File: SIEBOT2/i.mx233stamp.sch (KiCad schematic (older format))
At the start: 0 parts

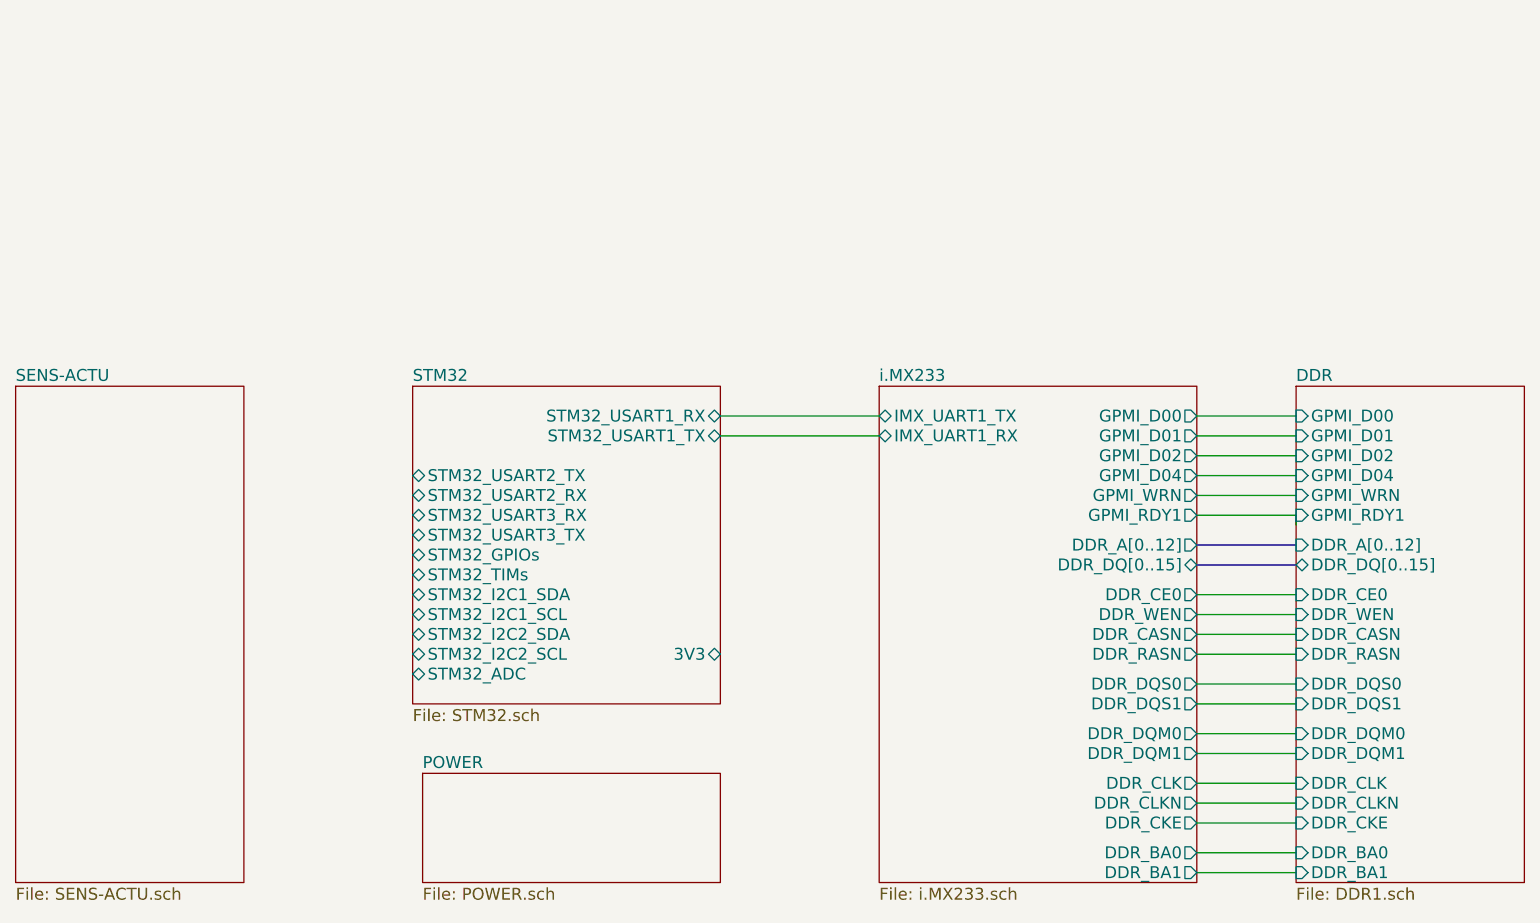
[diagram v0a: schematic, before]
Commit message: Added some fixes from AndroidStamp
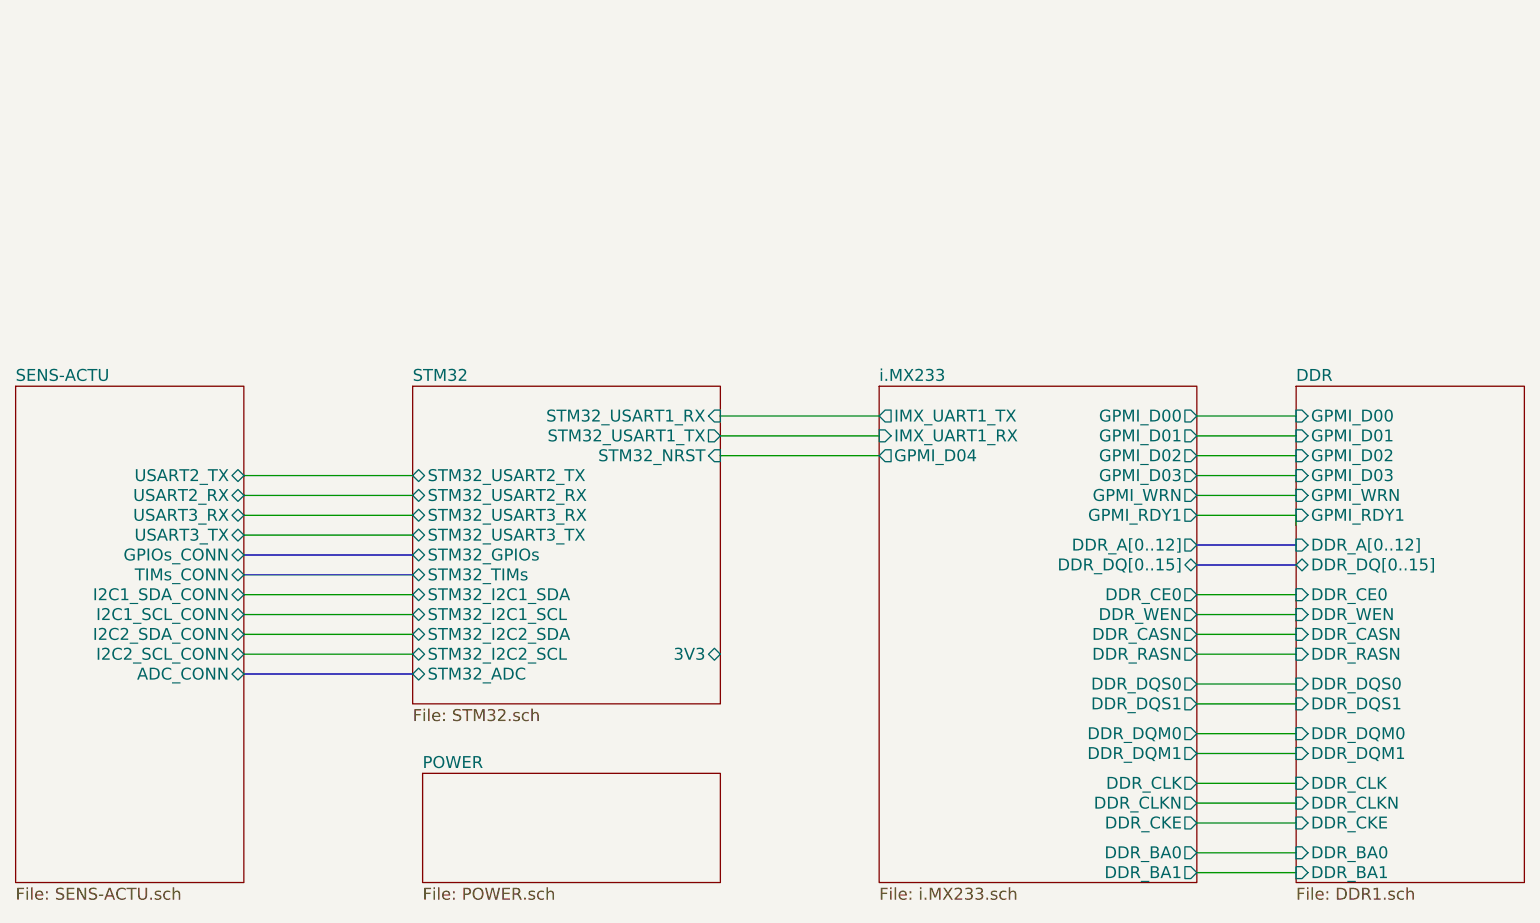
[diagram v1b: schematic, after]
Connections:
- wire segments 22 -> 31
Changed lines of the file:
@@
-EESchema Schematic File Version 2  date sáb 05 mar 2011 23:35:11 COT
+EESchema Schematic File Version 2  date jue 07 abr 2011 23:57:53 COT
 LIBS:stm32f100vxx
 LIBS:transistor-npn
@@
 LIBS:PROpendous-cache
 LIBS:w_analog
+LIBS:adm3101e
 LIBS:i.mx233stamp-cache
 EELAYER 25  0
@@
 Sheet 1 6
 Title ""
-Date "6 mar 2011"
+Date "8 apr 2011"
 Rev ""
 Comp ""
@@
 $EndDescr
 Wire Wire Line
+	6450 3250 5650 3250
+Wire Wire Line
+	3250 4250 4100 4250
+Wire Wire Line
+	4100 4050 3250 4050
+Wire Bus Line
+	4100 3750 3250 3750
+Wire Wire Line
+	4100 3650 3250 3650
+Wire Wire Line
+	4100 3450 3250 3450
+Wire Wire Line
 	5650 3150 6450 3150
 Wire Wire Line
@@
 Wire Wire Line
 	5650 3050 6450 3050
+Wire Wire Line
+	3250 3350 4100 3350
+Wire Wire Line
+	3250 3550 4100 3550
+Wire Bus Line
+	3250 3850 4100 3850
+Wire Wire Line
+	4100 3950 3250 3950
+Wire Wire Line
+	3250 4150 4100 4150
+Wire Bus Line
+	4100 4350 3250 4350
 $Sheet
 S 4100 2900 1550 1600
@@
 F0 "STM32" 60
 F1 "STM32.sch" 60
-F2 "STM32_USART1_RX" B R 5650 3050 60
+F2 "STM32_USART1_RX" I R 5650 3050 60
 F3 "STM32_ADC" B L 4100 4350 60
 F4 "3V3" B R 5650 4250 60
-F5 "STM32_USART1_TX" B R 5650 3150 60
+F5 "STM32_USART1_TX" O R 5650 3150 60
 F6 "STM32_I2C2_SCL" B L 4100 4250 60
 F7 "STM32_I2C2_SDA" B L 4100 4150 60
@@
 F14 "STM32_USART2_RX" B L 4100 3450 60
 F15 "STM32_USART2_TX" B L 4100 3350 60
+F16 "STM32_NRST" I R 5650 3250 60
 $EndSheet
 $Sheet
@@
 F0 "SENS-ACTU" 60
 F1 "SENS-ACTU.sch" 60
+F2 "USART3_RX" B R 3250 3550 60
+F3 "USART3_TX" B R 3250 3650 60
+F4 "USART2_TX" B R 3250 3350 60
+F5 "USART2_RX" B R 3250 3450 60
+F6 "GPIOs_CONN" B R 3250 3750 60
+F7 "TIMs_CONN" B R 3250 3850 60
+F8 "I2C2_SDA_CONN" B R 3250 4150 60
+F9 "I2C2_SCL_CONN" B R 3250 4250 60
+F10 "I2C1_SDA_CONN" B R 3250 3950 60
+F11 "I2C1_SCL_CONN" B R 3250 4050 60
+F12 "ADC_CONN" B R 3250 4350 60
 $EndSheet
 $Sheet
@@
 F15 "DDR_RASN" I L 8550 4250 60
 F16 "DDR_WEN" I L 8550 4050 60
-F17 "GPMI_D04" I L 8550 3350 60
+F17 "GPMI_D03" I L 8550 3350 60
 F18 "GPMI_D02" I L 8550 3250 60
 F19 "GPMI_WRN" I L 8550 3450 60
@@
 F15 "DDR_BA1" O R 8050 5350 60
 F16 "DDR_BA0" O R 8050 5250 60
-F17 "GPMI_D04" O R 8050 3350 60
+F17 "GPMI_D03" O R 8050 3350 60
 F18 "GPMI_WRN" O R 8050 3450 60
 F19 "GPMI_RDY1" O R 8050 3550 60
@@
 F21 "GPMI_D01" O R 8050 3150 60
 F22 "GPMI_D02" O R 8050 3250 60
-F23 "IMX_UART1_TX" B L 6450 3050 60
-F24 "IMX_UART1_RX" B L 6450 3150 60
+F23 "IMX_UART1_TX" O L 6450 3050 60
+F24 "IMX_UART1_RX" I L 6450 3150 60
+F25 "GPMI_D04" O L 6450 3250 60
 $EndSheet
 $EndSCHEMATC

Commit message: Added power dc-dc, fixed stm32 control pins
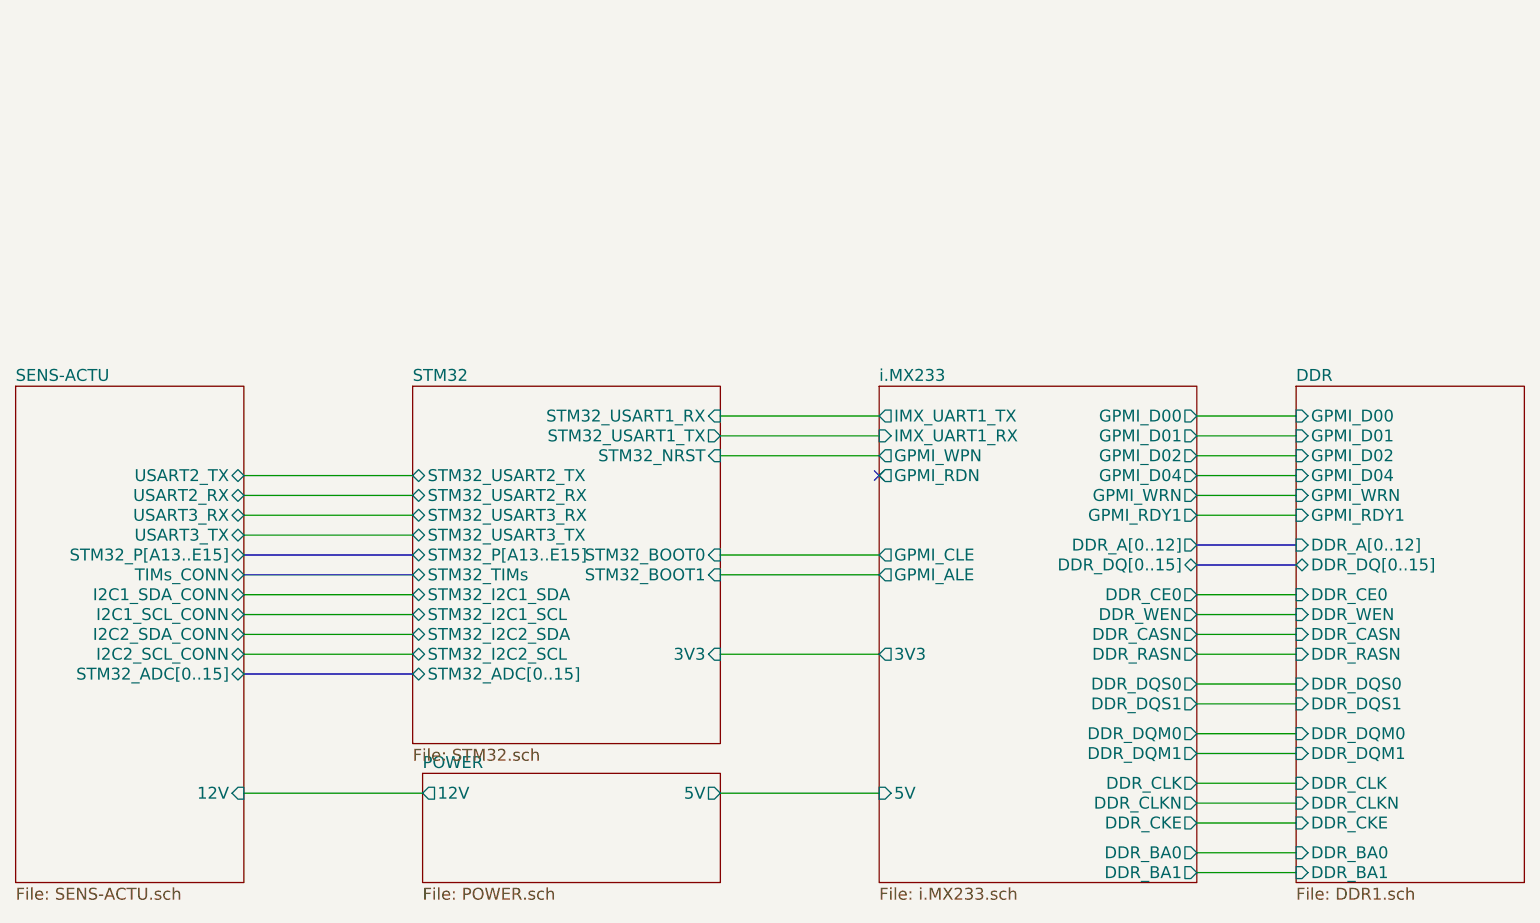
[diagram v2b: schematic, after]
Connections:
- no-connect marks 0 -> 1
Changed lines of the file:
@@
-EESchema Schematic File Version 2  date jue 07 abr 2011 23:57:53 COT
+EESchema Schematic File Version 2  date lun 11 abr 2011 13:13:06 COT
+LIBS:dc-dc
 LIBS:stm32f100vxx
 LIBS:transistor-npn
@@
 Sheet 1 6
 Title ""
-Date "8 apr 2011"
+Date "11 apr 2011"
 Rev ""
 Comp ""
@@
 $EndDescr
 Wire Wire Line
+	6450 4950 5650 4950
+Wire Wire Line
+	6450 4250 5650 4250
+Wire Wire Line
+	5650 3750 6450 3750
+Wire Bus Line
+	4100 4350 3250 4350
+Wire Wire Line
+	3250 4150 4100 4150
+Wire Wire Line
+	4100 3950 3250 3950
+Wire Bus Line
+	3250 3850 4100 3850
+Wire Wire Line
+	3250 3550 4100 3550
+Wire Wire Line
+	3250 3350 4100 3350
+Wire Wire Line
+	5650 3050 6450 3050
+Wire Wire Line
+	8550 3550 8050 3550
+Wire Wire Line
+	8550 3250 8050 3250
+Wire Wire Line
+	8550 3050 8050 3050
+Wire Bus Line
+	8550 3700 8050 3700
+Wire Wire Line
+	8050 4750 8550 4750
+Wire Wire Line
+	8550 4500 8050 4500
+Wire Wire Line
+	8050 4250 8550 4250
+Wire Wire Line
+	8050 5350 8550 5350
+Wire Wire Line
+	8050 5100 8550 5100
+Wire Wire Line
+	8050 4900 8550 4900
+Wire Wire Line
+	8050 4150 8550 4150
+Wire Wire Line
+	8050 4050 8550 4050
+Wire Wire Line
+	8050 3950 8550 3950
+Wire Wire Line
+	8050 5000 8550 5000
+Wire Wire Line
+	8050 5250 8550 5250
+Wire Wire Line
+	8050 4400 8550 4400
+Wire Wire Line
+	8550 4650 8050 4650
+Wire Wire Line
+	8050 3350 8550 3350
+Wire Bus Line
+	8050 3800 8550 3800
+Wire Wire Line
+	8050 3150 8550 3150
+Wire Wire Line
+	8050 3450 8550 3450
+Wire Wire Line
+	5650 3150 6450 3150
+Wire Wire Line
+	4100 3450 3250 3450
+Wire Wire Line
+	4100 3650 3250 3650
+Wire Bus Line
+	4100 3750 3250 3750
+Wire Wire Line
+	4100 4050 3250 4050
+Wire Wire Line
+	3250 4250 4100 4250
+Wire Wire Line
 	6450 3250 5650 3250
 Wire Wire Line
-	3250 4250 4100 4250
-Wire Wire Line
-	4100 4050 3250 4050
-Wire Bus Line
-	4100 3750 3250 3750
-Wire Wire Line
-	4100 3650 3250 3650
-Wire Wire Line
-	4100 3450 3250 3450
-Wire Wire Line
-	5650 3150 6450 3150
-Wire Wire Line
-	8050 3450 8550 3450
-Wire Wire Line
-	8050 3150 8550 3150
-Wire Bus Line
-	8050 3800 8550 3800
-Wire Wire Line
-	8050 3350 8550 3350
-Wire Wire Line
-	8550 4650 8050 4650
-Wire Wire Line
-	8050 4400 8550 4400
-Wire Wire Line
-	8050 5250 8550 5250
-Wire Wire Line
-	8050 5000 8550 5000
-Wire Wire Line
-	8050 3950 8550 3950
-Wire Wire Line
-	8050 4050 8550 4050
-Wire Wire Line
-	8050 4150 8550 4150
-Wire Wire Line
-	8050 4900 8550 4900
-Wire Wire Line
-	8050 5100 8550 5100
-Wire Wire Line
-	8050 5350 8550 5350
-Wire Wire Line
-	8050 4250 8550 4250
-Wire Wire Line
-	8550 4500 8050 4500
-Wire Wire Line
-	8050 4750 8550 4750
-Wire Bus Line
-	8550 3700 8050 3700
-Wire Wire Line
-	8550 3050 8050 3050
-Wire Wire Line
-	8550 3250 8050 3250
-Wire Wire Line
-	8550 3600 8550 3550
-Wire Wire Line
-	8550 3550 8050 3550
-Wire Wire Line
-	5650 3050 6450 3050
-Wire Wire Line
-	3250 3350 4100 3350
-Wire Wire Line
-	3250 3550 4100 3550
-Wire Bus Line
-	3250 3850 4100 3850
-Wire Wire Line
-	4100 3950 3250 3950
-Wire Wire Line
-	3250 4150 4100 4150
-Wire Bus Line
-	4100 4350 3250 4350
-$Sheet
-S 4100 2900 1550 1600
+	6450 3850 5650 3850
+Wire Wire Line
+	4150 4950 3250 4950
+NoConn ~ 6450 3350
+$Sheet
+S 4100 2900 1550 1800
 U 4D6EB053
 F0 "STM32" 60
 F1 "STM32.sch" 60
 F2 "STM32_USART1_RX" I R 5650 3050 60
-F3 "STM32_ADC" B L 4100 4350 60
-F4 "3V3" B R 5650 4250 60
-F5 "STM32_USART1_TX" O R 5650 3150 60
-F6 "STM32_I2C2_SCL" B L 4100 4250 60
-F7 "STM32_I2C2_SDA" B L 4100 4150 60
-F8 "STM32_I2C1_SDA" B L 4100 3950 60
-F9 "STM32_I2C1_SCL" B L 4100 4050 60
-F10 "STM32_TIMs" B L 4100 3850 60
-F11 "STM32_GPIOs" B L 4100 3750 60
-F12 "STM32_USART3_TX" B L 4100 3650 60
-F13 "STM32_USART3_RX" B L 4100 3550 60
-F14 "STM32_USART2_RX" B L 4100 3450 60
-F15 "STM32_USART2_TX" B L 4100 3350 60
-F16 "STM32_NRST" I R 5650 3250 60
+F3 "STM32_ADC[0..15]" B L 4100 4350 60
+F4 "STM32_USART1_TX" O R 5650 3150 60
+F5 "STM32_I2C2_SCL" B L 4100 4250 60
+F6 "STM32_I2C2_SDA" B L 4100 4150 60
+F7 "STM32_I2C1_SDA" B L 4100 3950 60
+F8 "STM32_I2C1_SCL" B L 4100 4050 60
+F9 "STM32_TIMs" B L 4100 3850 60
+F10 "STM32_P[A13..E15]" B L 4100 3750 60
+F11 "STM32_USART3_TX" B L 4100 3650 60
+F12 "STM32_USART3_RX" B L 4100 3550 60
+F13 "STM32_USART2_RX" B L 4100 3450 60
+F14 "STM32_USART2_TX" B L 4100 3350 60
+F15 "STM32_NRST" I R 5650 3250 60
+F16 "STM32_BOOT0" I R 5650 3750 60
+F17 "STM32_BOOT1" I R 5650 3850 60
+F18 "3V3" I R 5650 4250 60
 $EndSheet
 $Sheet
@@
 F4 "USART2_TX" B R 3250 3350 60
 F5 "USART2_RX" B R 3250 3450 60
-F6 "GPIOs_CONN" B R 3250 3750 60
+F6 "STM32_P[A13..E15]" B R 3250 3750 60
 F7 "TIMs_CONN" B R 3250 3850 60
 F8 "I2C2_SDA_CONN" B R 3250 4150 60
@@
 F10 "I2C1_SDA_CONN" B R 3250 3950 60
 F11 "I2C1_SCL_CONN" B R 3250 4050 60
-F12 "ADC_CONN" B R 3250 4350 60
+F12 "STM32_ADC[0..15]" B R 3250 4350 60
+F13 "12V" I R 3250 4950 60
 $EndSheet
 $Sheet
@@
 F0 "POWER" 60
 F1 "POWER.sch" 60
+F2 "12V" O L 4150 4950 60
+F3 "5V" O R 5650 4950 60
 $EndSheet
 $Sheet
@@
 F15 "DDR_RASN" I L 8550 4250 60
 F16 "DDR_WEN" I L 8550 4050 60
-F17 "GPMI_D03" I L 8550 3350 60
-F18 "GPMI_D02" I L 8550 3250 60
-F19 "GPMI_WRN" I L 8550 3450 60
-F20 "GPMI_RDY1" I L 8550 3550 60
-F21 "GPMI_D01" I L 8550 3150 60
-F22 "GPMI_D00" I L 8550 3050 60
+F17 "GPMI_D02" I L 8550 3250 60
+F18 "GPMI_WRN" I L 8550 3450 60
+F19 "GPMI_RDY1" I L 8550 3550 60
+F20 "GPMI_D01" I L 8550 3150 60
+F21 "GPMI_D00" I L 8550 3050 60
+F22 "GPMI_D04" I L 8550 3350 60
 $EndSheet
 $Sheet
@@
 F15 "DDR_BA1" O R 8050 5350 60
 F16 "DDR_BA0" O R 8050 5250 60
-F17 "GPMI_D03" O R 8050 3350 60
-F18 "GPMI_WRN" O R 8050 3450 60
-F19 "GPMI_RDY1" O R 8050 3550 60
-F20 "GPMI_D00" O R 8050 3050 60
-F21 "GPMI_D01" O R 8050 3150 60
-F22 "GPMI_D02" O R 8050 3250 60
-F23 "IMX_UART1_TX" O L 6450 3050 60
-F24 "IMX_UART1_RX" I L 6450 3150 60
-F25 "GPMI_D04" O L 6450 3250 60
+F17 "GPMI_WRN" O R 8050 3450 60
+F18 "GPMI_RDY1" O R 8050 3550 60
+F19 "GPMI_D00" O R 8050 3050 60
+F20 "GPMI_D01" O R 8050 3150 60
+F21 "GPMI_D02" O R 8050 3250 60
+F22 "IMX_UART1_TX" O L 6450 3050 60
+F23 "IMX_UART1_RX" I L 6450 3150 60
+F24 "GPMI_WPN" O L 6450 3250 60
+F25 "GPMI_RDN" O L 6450 3350 60
+F26 "GPMI_CLE" O L 6450 3750 60
+F27 "GPMI_ALE" O L 6450 3850 60
+F28 "GPMI_D04" O R 8050 3350 60
+F29 "3V3" O L 6450 4250 60
+F30 "5V" I L 6450 4950 60
 $EndSheet
 $EndSCHEMATC

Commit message: STM32 connection fixes + various fixes
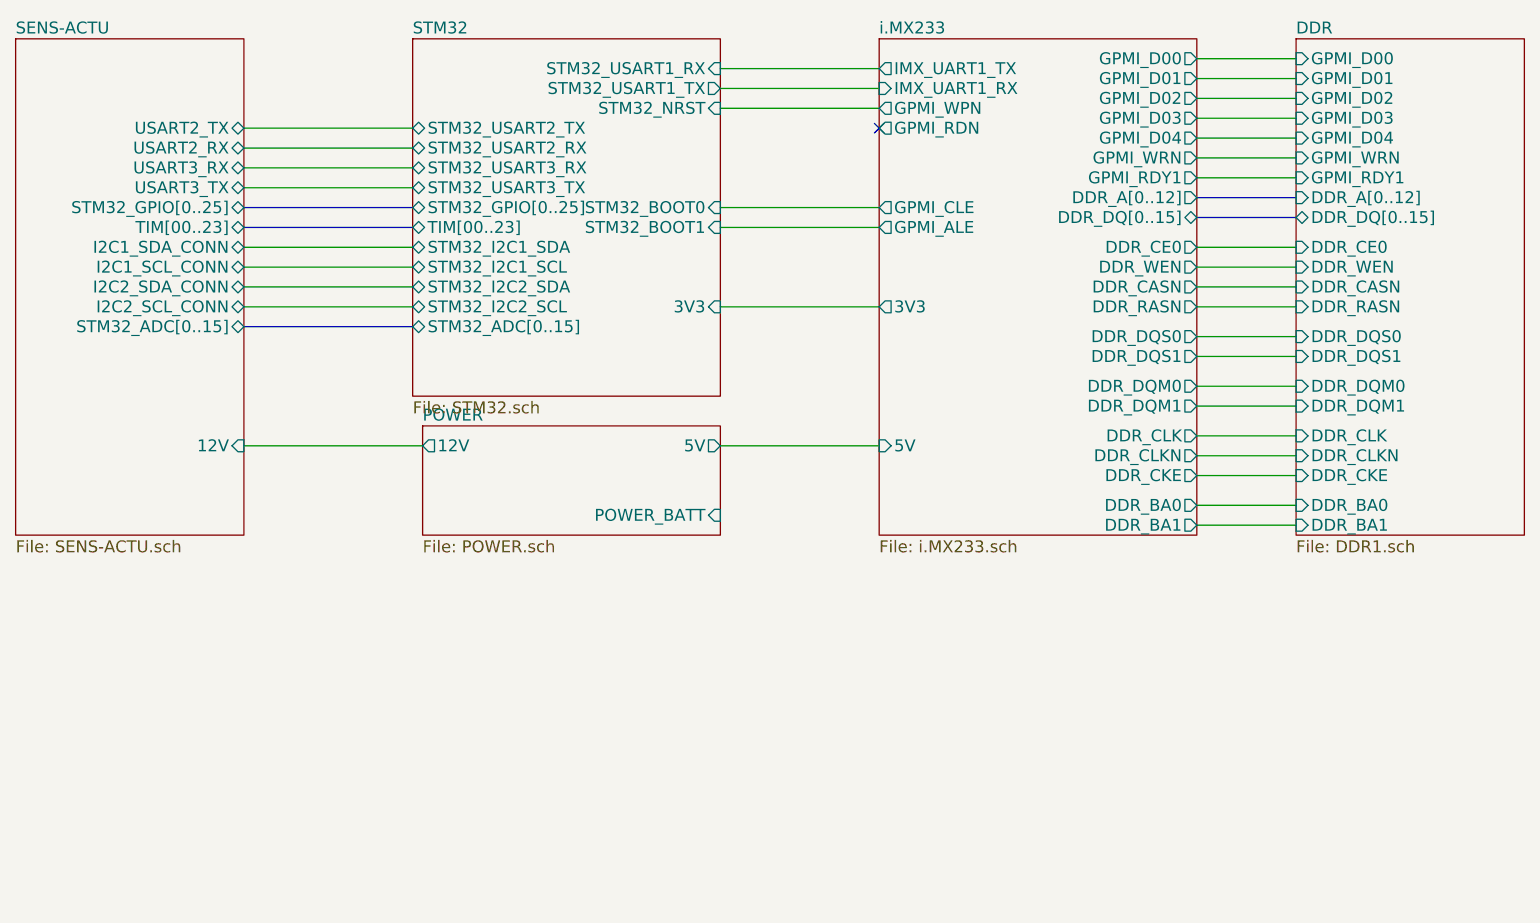
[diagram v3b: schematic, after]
